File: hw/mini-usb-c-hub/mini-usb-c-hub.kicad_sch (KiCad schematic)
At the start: 1 part, among them U101 FE1.1s

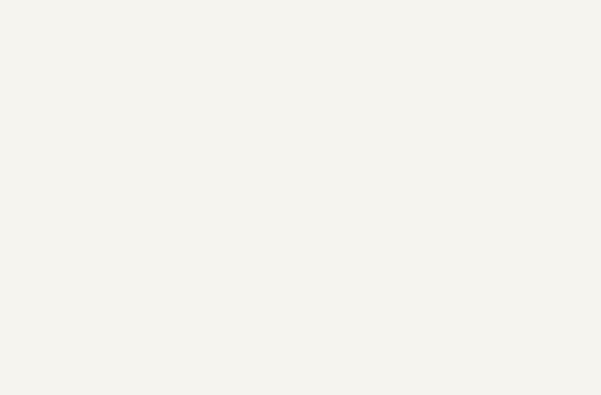
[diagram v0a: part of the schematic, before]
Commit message: chore(hw): choose usb-c receptacle
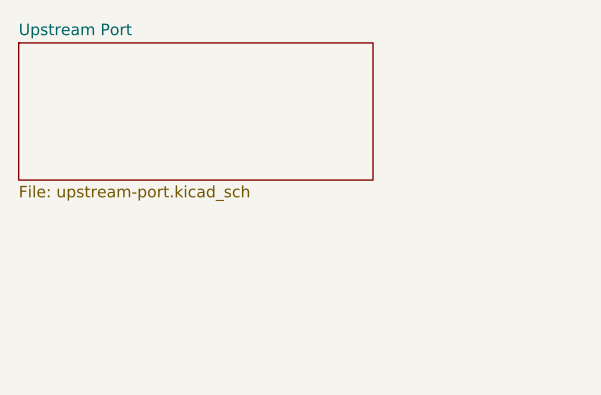
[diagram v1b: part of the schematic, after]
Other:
- added sheet Upstream Port (upstream-port.kicad_sch)
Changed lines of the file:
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@@
+		)
+	)
+	(sheet
+		(at 53.34 30.48)
+		(size 39.37 15.24)
+		(fields_autoplaced yes)
+		(stroke
+			(width 0.1524)
+			(type solid)
+		)
+		(fill
+			(color 0 0 0 0.0000)
+		)
+		(property "Sheetname" "Upstream Port"
+			(at 53.34 29.7684 0)
+			(effects
+				(font
+					(size 1.27 1.27)
+				)
+				(justify left bottom)
+			)
+		)
+		(property "Sheetfile" "upstream-port.kicad_sch"
+			(at 53.34 46.3046 0)
+			(effects
+				(font
+					(size 1.27 1.27)
+				)
+				(justify left top)
+			)
+		)
+		(instances
+			(project "mini-usb-c-hub"
+				(path "/7c04e056-0d84-4da3-ae50-c0eef25c6fa4"
+					(page "2")
+				)
+			)
 		)
 	)

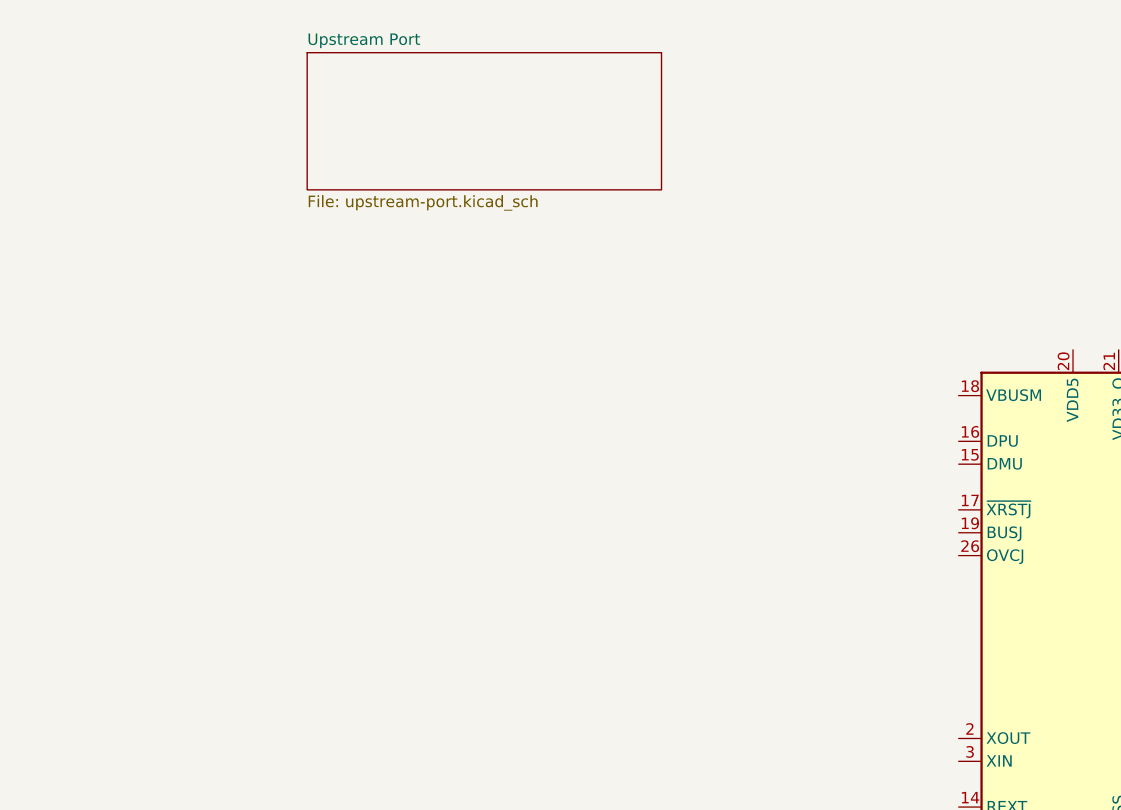
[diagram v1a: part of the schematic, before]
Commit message: chore(hw): add data pins, move upstream connector
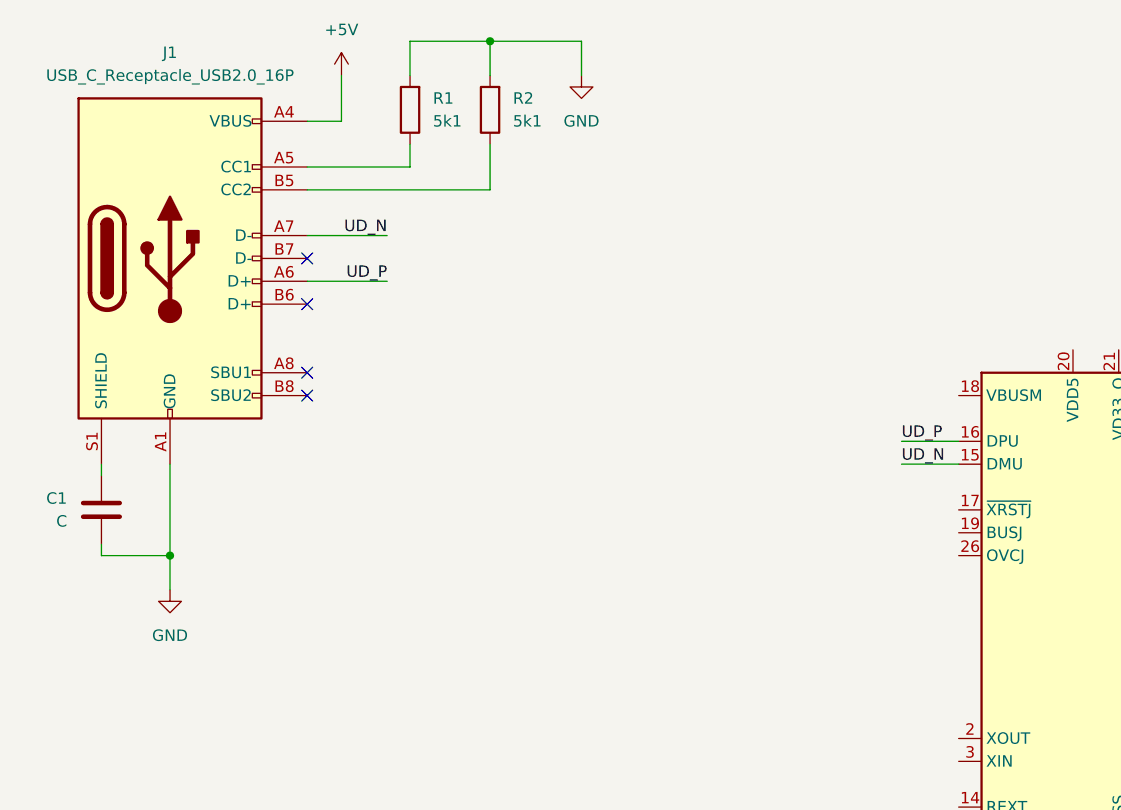
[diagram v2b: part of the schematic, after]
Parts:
- added C1: C, Capacitor_SMD:C_0805_2012Metric_Pad1.18x1.45mm_HandSolder, symbol Device:C
- added J1: USB_C_Receptacle_USB2.0_16P, local:USB_C_Receptacle_G-Switch_GT-USB-7010ASV_shortened, symbol Connector:USB_C_Receptacle_USB2.0_16P
- added R1, R2: 5k1, Resistor_SMD:R_0805_2012Metric_Pad1.20x1.40mm_HandSolder, symbol Device:R
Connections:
- net UD_N: now reaches U101.15 (DMU)
- net UD_N: now also J1.A7 (D-)
- net UD_P: now reaches U101.16 (DPU)
- net UD_P: now also J1.A6 (D+)
- new net: J1.A5 (CC1), R1.1
- new net: J1.B5 (CC2), R2.1
- new net: C1.2, J1.S1 (SHIELD)
- new net +5V: J1.A4 (VBUS), J1.A9 (VBUS), J1.B4 (VBUS), J1.B9 (VBUS)
- new net GND: C1.1, J1.A1 (GND), J1.A12 (GND), J1.B1 (GND), J1.B12 (GND), R1.2, R2.2
- no-connect marks 0 -> 4
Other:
- removed sheet Upstream Port

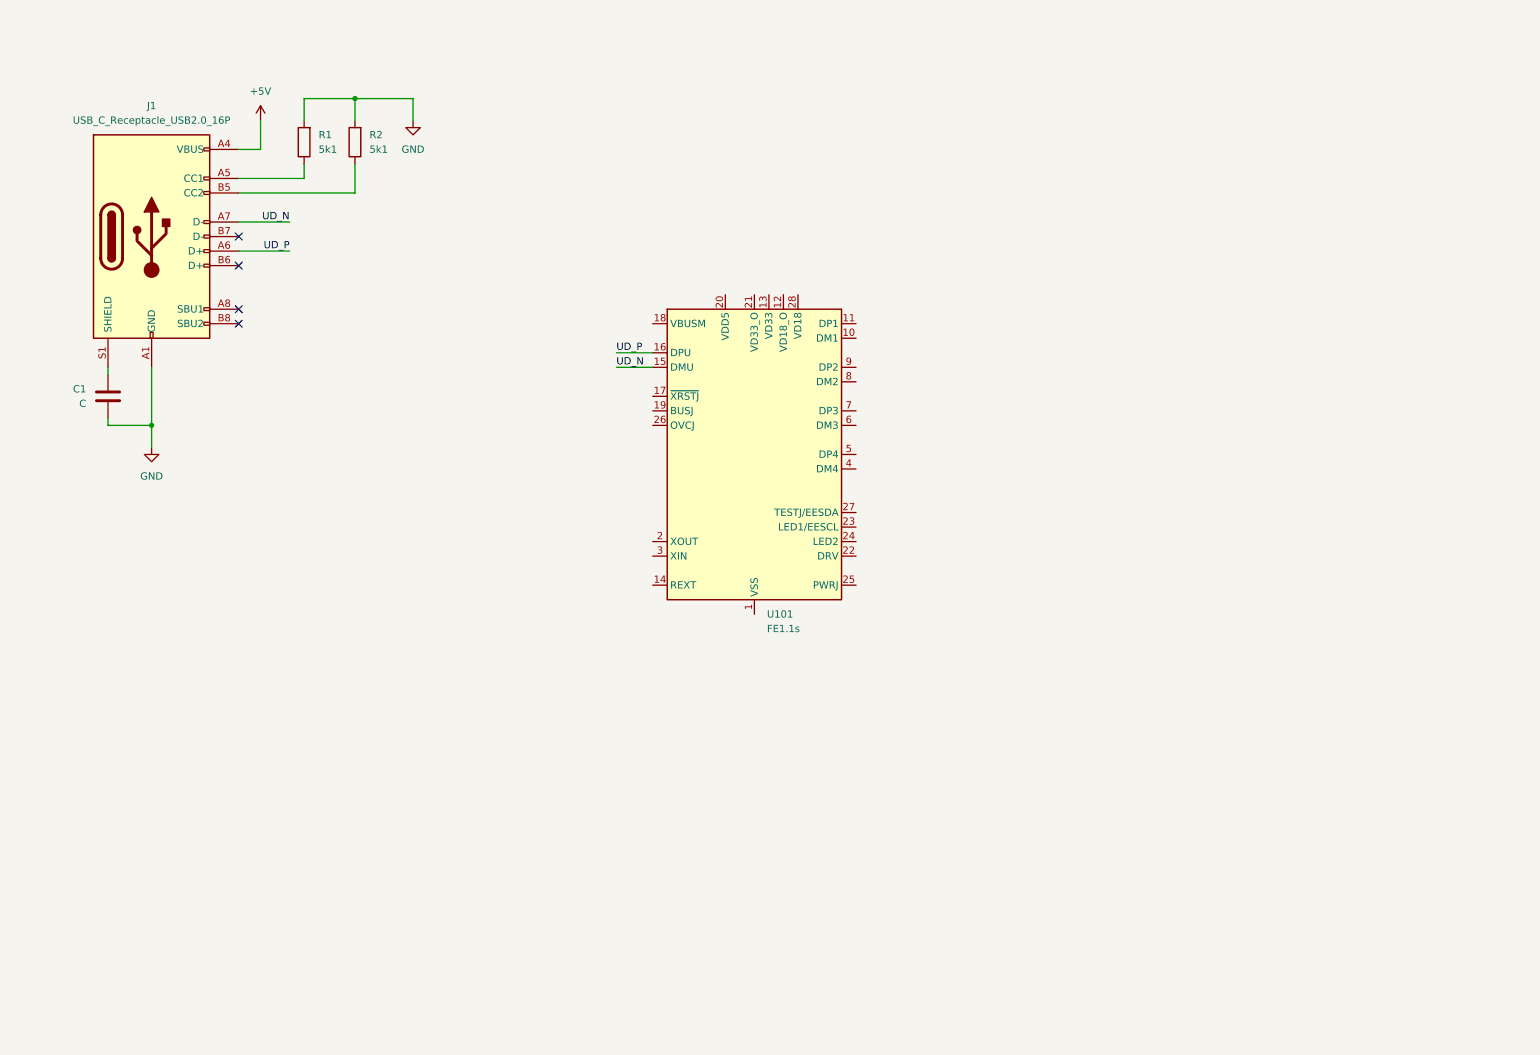
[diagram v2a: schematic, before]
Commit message: chore(hw): preliminary hub chip connections
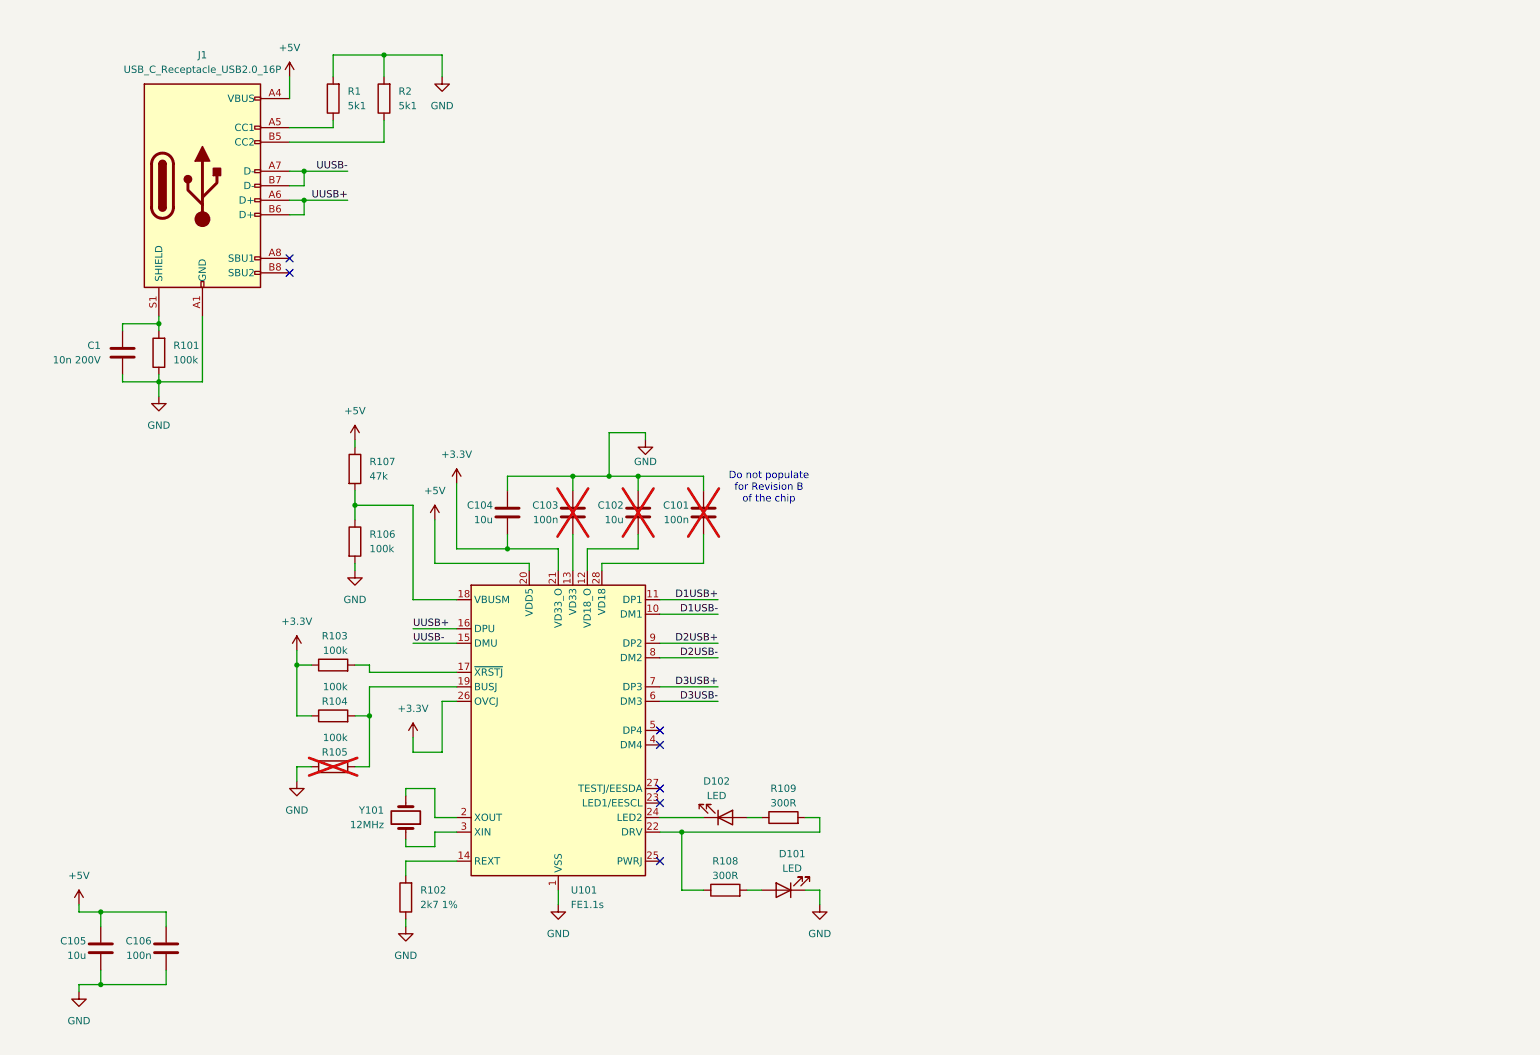
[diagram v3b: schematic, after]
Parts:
- added C101, C103, C106: 100n, Capacitor_SMD:C_0805_2012Metric_Pad1.18x1.45mm_HandSolder, symbol Device:C
- added C102, C104, C105: 10u, Capacitor_SMD:C_1206_3216Metric_Pad1.33x1.80mm_HandSolder, symbol Device:C
- added D101, D102: LED, symbol Device:LED
- added R101, R103, R104, R105, R106: 100k, Resistor_SMD:R_0805_2012Metric_Pad1.20x1.40mm_HandSolder, symbol Device:R
- added R102: 2k7 1%, Resistor_SMD:R_0805_2012Metric_Pad1.20x1.40mm_HandSolder, symbol Device:R
- added R107: 47k, Resistor_SMD:R_0805_2012Metric_Pad1.20x1.40mm_HandSolder, symbol Device:R
- added R108, R109: 300R, Resistor_SMD:R_0805_2012Metric_Pad1.20x1.40mm_HandSolder, symbol Device:R
- added Y101: 12MHz, symbol Device:Crystal
- C1: value C -> 10n 200V
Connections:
- net UD_N is gone; now on net UUSB-: J1.A7 (D-), U101.15 (DMU)
- net UD_P is gone; now on net UUSB+: J1.A6 (D+), U101.16 (DPU)
- net +5V: now also U101.20 (VDD5), C105.2, C106.2, R107.1
- net GND: now also U101.1 (VSS), C101.2, C102.2, C103.2, C104.2, C105.1, C106.1, D101.1 (K), R101.1, R102.1, R105.1, R106.2
- net UUSB+: now reaches J1.B6 (D+)
- net UUSB-: now reaches J1.B7 (D-)
- net at C1.2, J1.S1 (SHIELD): now also R101.2
- net D1USB-: now reaches U101.10 (DM1)
- net D1USB+: now reaches U101.11 (DP1)
- net at U101.12 (VD18_O): now also C102.1
- net at U101.13 (VD33): now also C103.1
- net at U101.14 (REXT): now also R102.2
- net at U101.17 (~{XRSTJ}): now also R103.2
- net at U101.18 (VBUSM): now also R106.1, R107.2
- net at U101.19 (BUSJ): now also R104.2, R105.2
- net at U101.2 (XOUT): now also Y101.2
- net +3.3V: now reaches U101.21 (VD33_O)
- net +3.3V: now also U101.26 (OVCJ), C104.1, R103.1, R104.1
- net at U101.22 (DRV): now also R108.1, R109.2
- net at U101.24 (LED2): now also D102.1 (K)
- net at U101.28 (VD18): now also C101.1
- net at U101.3 (XIN): now also Y101.1
- net D3USB-: now reaches U101.6 (DM3)
- net D3USB+: now reaches U101.7 (DP3)
- net D2USB-: now reaches U101.8 (DM2)
- net D2USB+: now reaches U101.9 (DP2)
- new net: D102.2 (A), R109.1
- new net: D101.2 (A), R108.2
- no-connect marks 4 -> 7
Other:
- note added: "Do not populate for Revision B of the chip"
- moved on the sheet: C1, J1, R1, R2, U101

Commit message: chore(hw): update power supply and add some notes
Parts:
- removed R107: 47k, Resistor_SMD:R_0805_2012Metric_Pad1.20x1.40mm_HandSolder, symbol Device:R
- added C2, C3: 10p, Capacitor_SMD:C_1206_3216Metric_Pad1.33x1.80mm_HandSolder, symbol Device:C
- added D1: PRTR5V0U2X, Package_TO_SOT_SMD:SOT-143, symbol Power_Protection:PRTR5V0U2X
- added R3: 0R, Resistor_SMD:R_0805_2012Metric_Pad1.20x1.40mm_HandSolder, symbol Device:R
- C103: now fitted
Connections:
- net +5V: now also R103.1, R104.1, R106.1, U101.26 (OVCJ)
- net GND: now also C2.1, C3.1; no longer R106.2
- net at C102.1, U101.12 (VD18_O): now also R3.1
- net at C103.1, U101.13 (VD33): now also C104.1, U101.21 (VD33_O)
- net at U101.3 (XIN), Y101.1: now also C3.2
- net at U101.2 (XOUT), Y101.2: now also C2.2
- net at U101.18 (VBUSM): now also R106.2; no longer R106.1
- net at C101.1, U101.28 (VD18): now also R3.2
- removed net +3.3V: C104.1, R103.1, R104.1, U101.21 (VD33_O), U101.26 (OVCJ)
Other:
- note added: "Should be 3v3?"
- note added: "The capacitors and resistor should be unpopulated when Revision B of the chip is used"
- note removed: "Do not populate for Revision B of the chip"
- moved on the sheet: C101, C102, C104, D101, R102, R103, R104, R105, R106, R108
